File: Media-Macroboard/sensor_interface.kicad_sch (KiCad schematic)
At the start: 30 parts, among them J3 Conn_01x04_MountingPin, Q4 TEMT6000X01, SW1 SW_MEC_5G, SW12 SW_MEC_5G, SW2 SW_MEC_5G, SW3 SW_MEC_5G, SW4 SW_MEC_5G, SW5 SW_MEC_5G, SW6 SW_MEC_5G, SW7 SW_MEC_5G, SW8 SW_MEC_5G, SW9 SW_MEC_5G

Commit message: First productable version
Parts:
- added R23, R24, R25: 470, Resistor_SMD:R_0805_2012Metric_Pad1.20x1.40mm_HandSolder, symbol Device:R
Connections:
- net GND: now also R23.2, R24.2, R25.2
- new net: LED10.1 (K), R25.1
- new net: LED8.1 (K), R23.1
- new net: LED7.1 (K), R19.1
- new net: LED9.1 (K), R24.1
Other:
- note added: "JoyStick"

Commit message: Update
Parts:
- SW1: footprint PCM_Switch_Keyboard_Cherry_MX:SW_Cherry_MX_PCB_1.00u -> PCM_Switch_Keyboard_Cherry_MX:SW_Cherry_Compact
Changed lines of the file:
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@@
 			)
 		)
-		(property "Footprint" "PCM_Switch_Keyboard_Cherry_MX:SW_Cherry_MX_PCB_1.00u"
+		(property "Footprint" "PCM_Switch_Keyboard_Cherry_MX:SW_Cherry_Compact"
 			(at 39.37 35.56 0)
 			(effects

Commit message: Made four-layer version
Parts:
- removed LED10, LED7, LED8, LED9: LTST-C170TBKT, Footprints:LEDC2012X120N, symbol LTST-C170TBKT:LTST-C170TBKT
- removed Q4: TEMT6000X01, Footprints:TEMT6000X01, symbol TEMT6000X01:TEMT6000X01
- removed R19, R23, R24, R25: 470, Resistor_SMD:R_0805_2012Metric_Pad1.20x1.40mm_HandSolder, symbol Device:R
- removed R21: 10K, Resistor_SMD:R_0805_2012Metric_Pad1.20x1.40mm_HandSolder, symbol Device:R
- SW12, SW2, SW3, SW4, SW5, SW6, SW7, SW8, SW9: footprint PCM_Switch_Keyboard_Cherry_MX:SW_Cherry_MX_PCB_1.00u -> PCM_Switch_Keyboard_Cherry_MX:SW_Cherry_Compact
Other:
- note removed: "LED"
- note removed: "Light Sensor"

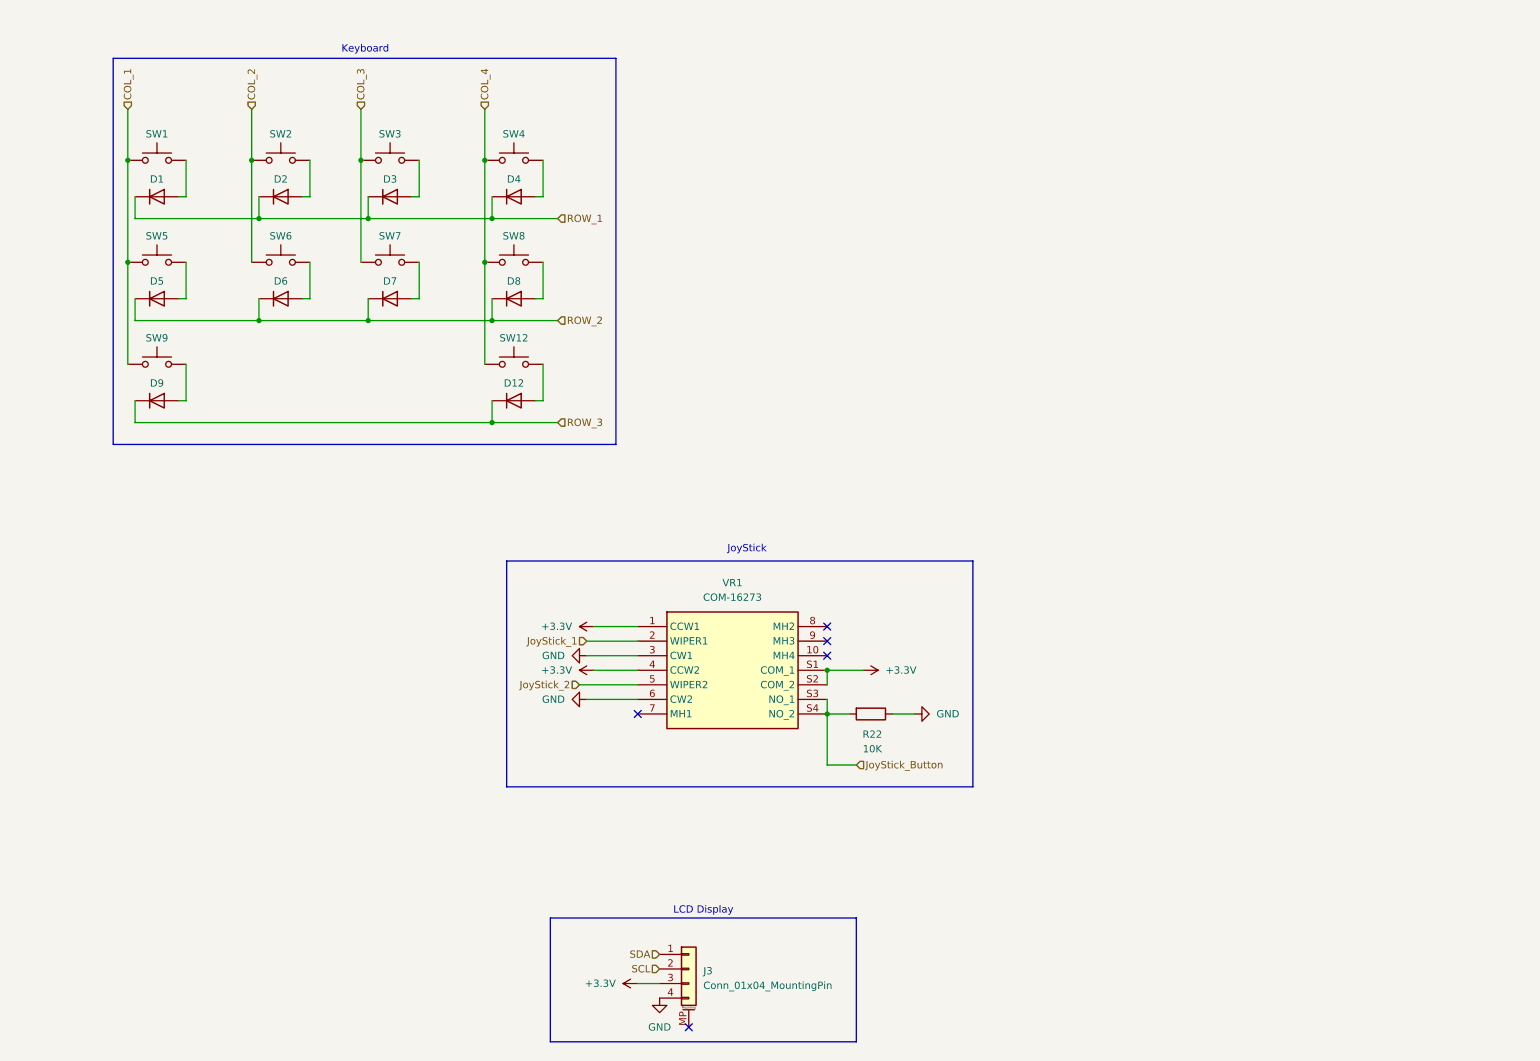
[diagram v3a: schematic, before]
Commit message: Added more rows and columns
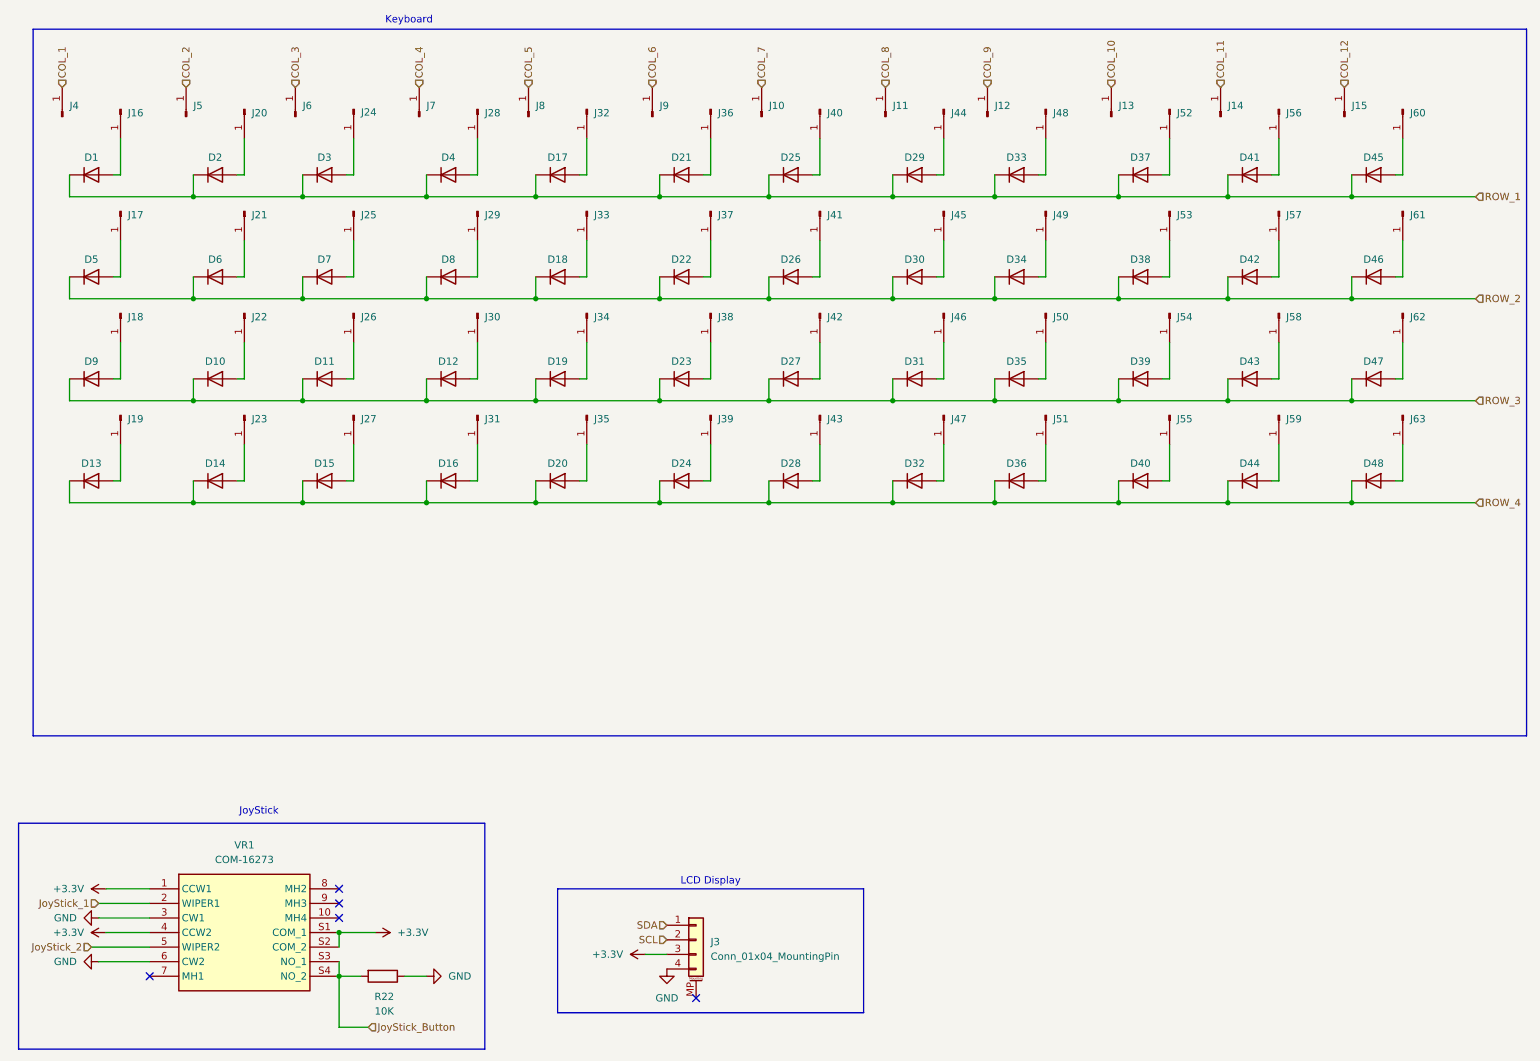
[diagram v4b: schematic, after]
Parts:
- removed SW1, SW12, SW2, SW3, SW4, SW5, SW6, SW7, SW8, SW9: SW_MEC_5G, PCM_Switch_Keyboard_Cherry_MX:SW_Cherry_Compact, symbol Switch:SW_MEC_5G
- added D10, D11, D13, D14, D15, D16, D17, D18, D19, D20, D21, D22, D23, D24, D25, D26, D27, D28, D29, D30, D31, D32, D33, D34, D35, D36, D37, D38, D39, D40, D41, D42, D43, D44, D45, D46, D47, D48: D, Diode_SMD:D_0805_2012Metric_Pad1.15x1.40mm_HandSolder, symbol Device:D
- added J10, J11, J12, J13, J14, J15, J16, J17, J18, J19, J20, J21, J22, J23, J24, J25, J26, J27, J28, J29, J30, J31, J32, J33, J34, J35, J36, J37, J38, J39, J4, J40, J41, J42, J43, J44, J45, J46, J47, J48, J49, J5, J50, J51, J52, J53, J54, J55, J56, J57, J58, J59, J6, J60, J61, J62, J63, J7, J8, J9: Conn_01x01_Pin, Connector_PinHeader_1.00mm:PinHeader_1x01_P1.00mm_Vertical, symbol Connector:Conn_01x01_Pin
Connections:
- net COL_1: now also J4.1 (Pin_1)
- net COL_2: now also J5.1 (Pin_1)
- net COL_3: now also J6.1 (Pin_1)
- net COL_4: now also J7.1 (Pin_1)
- net ROW_1: now also D17.1 (K), D21.1 (K), D25.1 (K), D29.1 (K), D33.1 (K), D37.1 (K), D41.1 (K), D45.1 (K)
- net ROW_2: now also D18.1 (K), D22.1 (K), D26.1 (K), D30.1 (K), D34.1 (K), D38.1 (K), D42.1 (K), D46.1 (K)
- net ROW_3: now also D10.1 (K), D11.1 (K), D19.1 (K), D23.1 (K), D27.1 (K), D31.1 (K), D35.1 (K), D39.1 (K), D43.1 (K), D47.1 (K)
- net at D5.2 (A): now also J17.1 (Pin_1)
- net at D9.2 (A): now also J18.1 (Pin_1)
- net at D8.2 (A): now also J29.1 (Pin_1)
- net at D1.2 (A): now also J16.1 (Pin_1)
- net at D4.2 (A): now also J28.1 (Pin_1)
- net at D7.2 (A): now also J25.1 (Pin_1)
- net at D12.2 (A): now also J30.1 (Pin_1)
- net at D2.2 (A): now also J20.1 (Pin_1)
- net at D3.2 (A): now also J24.1 (Pin_1)
- net at D6.2 (A): now also J21.1 (Pin_1)
- new net: D30.2 (A), J45.1 (Pin_1)
- new net: D45.2 (A), J60.1 (Pin_1)
- new net: D18.2 (A), J33.1 (Pin_1)
- new net: D24.2 (A), J39.1 (Pin_1)
- new net: D34.2 (A), J49.1 (Pin_1)
- new net: D46.2 (A), J61.1 (Pin_1)
- new net: D31.2 (A), J46.1 (Pin_1)
- new net: D41.2 (A), J56.1 (Pin_1)
- new net: D21.2 (A), J36.1 (Pin_1)
- new net: D43.2 (A), J58.1 (Pin_1)
- new net: D44.2 (A), J59.1 (Pin_1)
- new net: D40.2 (A), J55.1 (Pin_1)
- new net: D36.2 (A), J51.1 (Pin_1)
- new net: D22.2 (A), J37.1 (Pin_1)
- new net: D19.2 (A), J34.1 (Pin_1)
- new net: D16.2 (A), J31.1 (Pin_1)
- new net: D15.2 (A), J27.1 (Pin_1)
- new net: D25.2 (A), J40.1 (Pin_1)
- new net: D38.2 (A), J53.1 (Pin_1)
- new net: D10.2 (A), J22.1 (Pin_1)
- new net: D35.2 (A), J50.1 (Pin_1)
- new net: D17.2 (A), J32.1 (Pin_1)
- new net: D33.2 (A), J48.1 (Pin_1)
- new net: D23.2 (A), J38.1 (Pin_1)
- new net: D47.2 (A), J62.1 (Pin_1)
- new net: D13.2 (A), J19.1 (Pin_1)
- new net: D14.2 (A), J23.1 (Pin_1)
- new net: D42.2 (A), J57.1 (Pin_1)
- new net: D37.2 (A), J52.1 (Pin_1)
- new net: D39.2 (A), J54.1 (Pin_1)
- new net: D20.2 (A), J35.1 (Pin_1)
- new net: D11.2 (A), J26.1 (Pin_1)
- new net: D29.2 (A), J44.1 (Pin_1)
- new net: D27.2 (A), J42.1 (Pin_1)
- new net: D48.2 (A), J63.1 (Pin_1)
- new net: D28.2 (A), J43.1 (Pin_1)
- new net: D32.2 (A), J47.1 (Pin_1)
- new net: D26.2 (A), J41.1 (Pin_1)
- new net COL_10: J13.1 (Pin_1)
- new net COL_11: J14.1 (Pin_1)
- new net COL_12: J15.1 (Pin_1)
- new net COL_5: J8.1 (Pin_1)
- new net COL_6: J9.1 (Pin_1)
- new net COL_7: J10.1 (Pin_1)
- new net COL_8: J11.1 (Pin_1)
- new net COL_9: J12.1 (Pin_1)
- new net ROW_4: D13.1 (K), D14.1 (K), D15.1 (K), D16.1 (K), D20.1 (K), D24.1 (K), D28.1 (K), D32.1 (K), D36.1 (K), D40.1 (K), D44.1 (K), D48.1 (K)
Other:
- moved on the sheet: D1, D12, D2, D3, D4, D5, D6, D7, D8, D9, J3, R22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
